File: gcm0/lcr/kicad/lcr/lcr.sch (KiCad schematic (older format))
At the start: 82 parts, among them Q1 BC547, Q2 BC547, Q3 BC547, Q4 BC547, Q5 BC547, SW1 SW_Push, SW2 SW_Push, U1 L7805, U10 NE5532, U10 TL084, U11 CD4053B, U2 L7905, U3 LM1117-3.3, U4 74HC595, U5 STM32F030F4P6, U7 CD4052B, U8 NE5532, U9 NE5532, Y1 8M

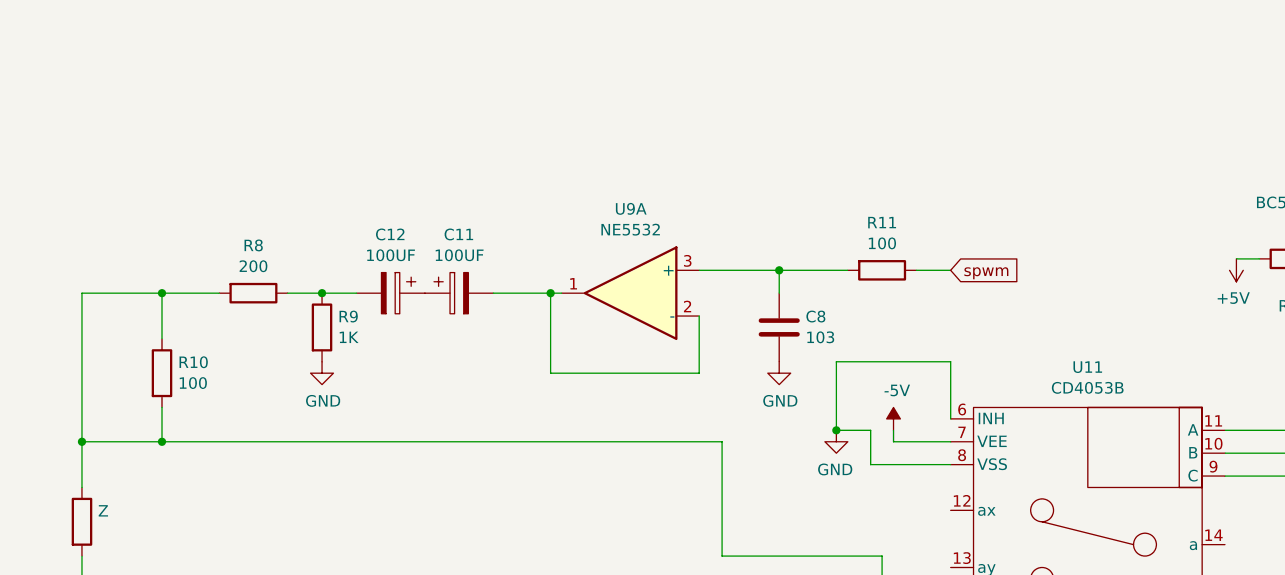
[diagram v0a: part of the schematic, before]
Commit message: 修改阻抗计算函数
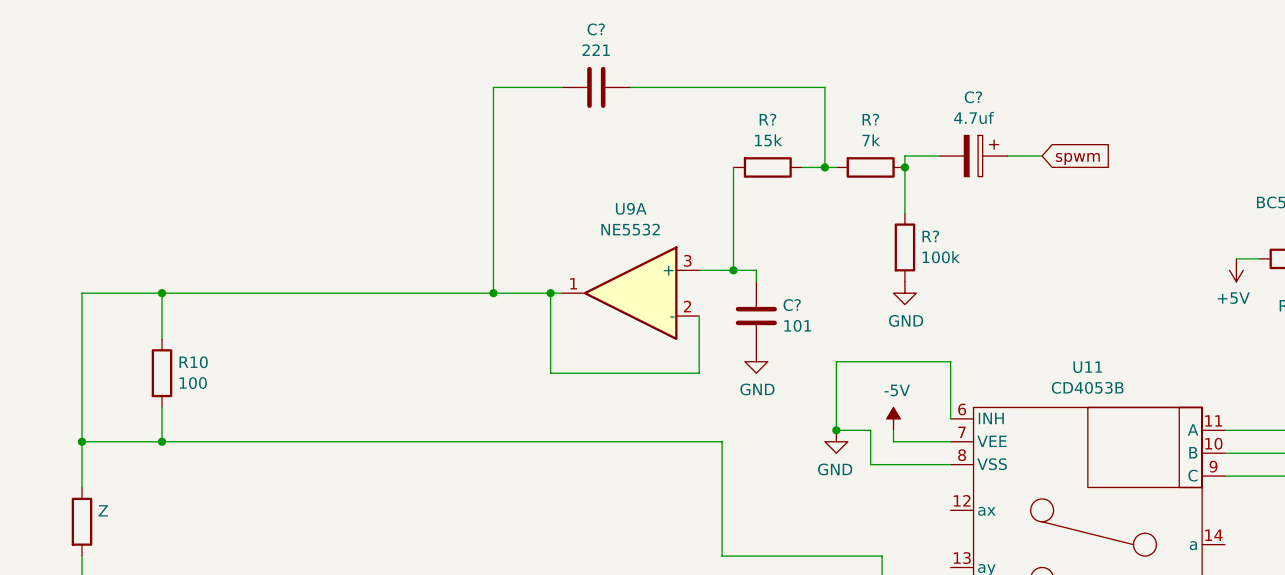
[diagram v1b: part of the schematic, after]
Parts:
- removed C11, C12: 100UF, symbol Device:CP
- removed C8: 103, symbol Device:C
- removed R11: 100, symbol Device:R
- removed R8: 200, symbol Device:R
- removed R9: 1K, symbol Device:R
- added C?: 101, symbol Device:C
- added C?: 221, symbol Device:C
- added C?: 4.7uf, symbol Device:CP
- added R?: 15k, symbol Device:R
- added R?: 7k, symbol Device:R
- added R?: 100k, symbol Device:R
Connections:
- net GND: now also C?.2, R?.2
- net spwm: now also C?.1
- net at R10.1, R10.2, U11.2 (bx)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: now also U9.1, U9.2 (-), C?.2
- net at U9.3 (+): now also C?.1, R?.2
- new net: C?.1, R?.1, R?.2
- new net: C?.2, R?.1, R?.1
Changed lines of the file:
@@
 	1250 2300 1250 2450
 Connection ~ 2050 3150
-$Comp
-L Device:CP C11
-U 1 1 5DB73CA6
-P 2550 1800
-F 0 "C11" V 2295 1800 50  0000 C CNN
-F 1 "100UF" V 2386 1800 50  0000 C CNN
-F 2 "" H 2588 1650 50  0001 C CNN
-F 3 "~" H 2550 1800 50  0001 C CNN
-	1    2550 1800
-	0    -1   1    0
-$EndComp
-$Comp
-L Device:CP C12
-U 1 1 5DB75C4D
-P 2250 1800
-F 0 "C12" V 1995 1800 50  0000 C CNN
-F 1 "100UF" V 2086 1800 50  0000 C CNN
-F 2 "" H 2288 1650 50  0001 C CNN
-F 3 "~" H 2250 1800 50  0001 C CNN
-	1    2250 1800
-	0    1    1    0
-$EndComp
 Wire Wire Line
 	3000 1800 2950 1800
-$Comp
-L Device:R R9
-U 1 1 5DBA1D7C
-P 1950 1950
-F 0 "R9" H 2020 1996 50  0000 L CNN
-F 1 "1K" H 2020 1905 50  0000 L CNN
-F 2 "" V 1880 1950 50  0001 C CNN
-F 3 "~" H 1950 1950 50  0001 C CNN
-	1    1950 1950
-	1    0    0    -1
-$EndComp
-$Comp
-L Device:R R8
-U 1 1 5DBA3300
-P 1650 1800
-F 0 "R8" V 1443 1800 50  0000 C CNN
-F 1 "200" V 1534 1800 50  0000 C CNN
-F 2 "" V 1580 1800 50  0001 C CNN
-F 3 "~" H 1650 1800 50  0001 C CNN
-	1    1650 1800
-	0    1    1    0
-$EndComp
-Wire Wire Line
-	2100 1800 1950 1800
-Wire Wire Line
-	1950 1800 1800 1800
-Connection ~ 1950 1800
 Wire Wire Line
 	3600 1900 3600 2150
@@
 $Comp
 L power:GND #PWR?
-U 1 1 5DBEFC51
-P 1950 2100
-F 0 "#PWR?" H 1950 1850 50  0001 C CNN
-F 1 "GND" H 1955 1927 50  0000 C CNN
-F 2 "" H 1950 2100 50  0001 C CNN
-F 3 "" H 1950 2100 50  0001 C CNN
-	1    1950 2100
-	1    0    0    -1
-$EndComp
-$Comp
-L power:GND #PWR?
 U 1 1 5DBF1737
-P 3950 2100
-F 0 "#PWR?" H 3950 1850 50  0001 C CNN
-F 1 "GND" H 3955 1927 50  0000 C CNN
-F 2 "" H 3950 2100 50  0001 C CNN
-F 3 "" H 3950 2100 50  0001 C CNN
-	1    3950 2100
-	1    0    0    -1
-$EndComp
-$Comp
-L Device:C C8
-U 1 1 5DBF3A78
-P 3950 1950
-F 0 "C8" H 4065 1996 50  0000 L CNN
-F 1 "103" H 4065 1905 50  0000 L CNN
-F 2 "" H 3988 1800 50  0001 C CNN
-F 3 "~" H 3950 1950 50  0001 C CNN
-	1    3950 1950
-	1    0    0    -1
-$EndComp
-Wire Wire Line
-	3600 1700 3950 1700
-Wire Wire Line
-	3950 1700 3950 1800
-$Comp
-L Device:R R11
-U 1 1 5DC0413C
-P 4400 1700
-F 0 "R11" V 4193 1700 50  0000 C CNN
-F 1 "100" V 4284 1700 50  0000 C CNN
-F 2 "" V 4330 1700 50  0001 C CNN
-F 3 "~" H 4400 1700 50  0001 C CNN
-	1    4400 1700
-	0    1    1    0
-$EndComp
-Wire Wire Line
-	4250 1700 3950 1700
-Connection ~ 3950 1700
-Wire Wire Line
-	1500 1800 1250 1800
+P 3850 2050
+F 0 "#PWR?" H 3850 1800 50  0001 C CNN
+F 1 "GND" H 3855 1877 50  0000 C CNN
+F 2 "" H 3850 2050 50  0001 C CNN
+F 3 "" H 3850 2050 50  0001 C CNN
+	1    3850 2050
+	1    0    0    -1
+$EndComp
 Wire Wire Line
 	1250 1800 1250 2000
-Text GLabel 4700 1700 2    50   Input ~ 0
+Text GLabel 5100 1200 2    50   Input ~ 0
 spwm
 Wire Wire Line
-	4700 1700 4550 1700
+	5100 1200 4950 1200
 Text GLabel 14700 8100 2    50   Input ~ 0
 ADC1
@@
 Wire Wire Line
 	900  1800 900  2450
-Connection ~ 1250 1800
 Wire Wire Line
 	1250 2450 900  2450
@@
 	12550 4000 12550 4250
 Connection ~ 12550 4250
+$Comp
+L Device:R R?
+U 1 1 5D991ACB
+P 3900 1250
+F 0 "R?" V 3693 1250 50  0000 C CNN
+F 1 "15k" V 3784 1250 50  0000 C CNN
+F 2 "" V 3830 1250 50  0001 C CNN
+F 3 "~" H 3900 1250 50  0001 C CNN
+	1    3900 1250
+	0    1    1    0
+$EndComp
+$Comp
+L Device:R R?
+U 1 1 5D993C65
+P 4350 1250
+F 0 "R?" V 4143 1250 50  0000 C CNN
+F 1 "7k" V 4234 1250 50  0000 C CNN
+F 2 "" V 4280 1250 50  0001 C CNN
+F 3 "~" H 4350 1250 50  0001 C CNN
+	1    4350 1250
+	0    1    1    0
+$EndComp
+$Comp
+L Device:R R?
+U 1 1 5D9B1D5F
+P 4500 1600
+F 0 "R?" H 4570 1646 50  0000 L CNN
+F 1 "100k" H 4570 1555 50  0000 L CNN
+F 2 "" V 4430 1600 50  0001 C CNN
+F 3 "~" H 4500 1600 50  0001 C CNN
+	1    4500 1600
+	1    0    0    -1
+$EndComp
+$Comp
+L Device:C C?
+U 1 1 5D9E9F87
+P 3850 1900
+F 0 "C?" H 3965 1946 50  0000 L CNN
+F 1 "101" H 3965 1855 50  0000 L CNN
+F 2 "" H 3888 1750 50  0001 C CNN
+F 3 "~" H 3850 1900 50  0001 C CNN
+	1    3850 1900
+	1    0    0    -1
+$EndComp
+Wire Wire Line
+	3850 1700 3850 1750
+Wire Wire Line
+	3750 1250 3750 1700
+Wire Wire Line
+	3600 1700 3750 1700
+Connection ~ 3750 1700
+Wire Wire Line
+	3750 1700 3850 1700
+Wire Wire Line
+	4050 1250 4150 1250
+Wire Wire Line
+	4500 1250 4500 1450
+$Comp
+L Device:C C?
+U 1 1 5DA7AEC8
+P 3150 900
+F 0 "C?" V 2898 900 50  0000 C CNN
+F 1 "221" V 2989 900 50  0000 C CNN
+F 2 "" H 3188 750 50  0001 C CNN
+F 3 "~" H 3150 900 50  0001 C CNN
+	1    3150 900
+	0    1    1    0
+$EndComp
+Wire Wire Line
+	3300 900  4150 900
+Wire Wire Line
+	4150 900  4150 1250
+Connection ~ 4150 1250
+Wire Wire Line
+	4150 1250 4200 1250
+Wire Wire Line
+	3000 900  2700 900
+Wire Wire Line
+	2700 900  2700 1800
+Wire Wire Line
+	1250 1800 2700 1800
+Connection ~ 1250 1800
+Connection ~ 2700 1800
+$Comp
+L Device:CP C?
+U 1 1 5DAF3F4F
+P 4800 1200
+F 0 "C?" V 4545 1200 50  0000 C CNN
+F 1 "4.7uf" V 4636 1200 50  0000 C CNN
+F 2 "" H 4838 1050 50  0001 C CNN
+F 3 "~" H 4800 1200 50  0001 C CNN
+	1    4800 1200
+	0    1    1    0
+$EndComp
+Wire Wire Line
+	4650 1200 4500 1200
+Wire Wire Line
+	4500 1200 4500 1250
+Connection ~ 4500 1250
+$Comp
+L power:GND #PWR?
+U 1 1 5DB3405A
+P 4500 1750
+F 0 "#PWR?" H 4500 1500 50  0001 C CNN
+F 1 "GND" H 4505 1577 50  0000 C CNN
+F 2 "" H 4500 1750 50  0001 C CNN
+F 3 "" H 4500 1750 50  0001 C CNN
+	1    4500 1750
+	1    0    0    -1
+$EndComp
 $EndSCHEMATC

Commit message: 试验设置几个量程
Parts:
- added R8: 390, symbol Device:R
- R17: value 1k -> 390
- gave numbers to parts that had none: 6
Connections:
- net at R10.1, R10.2, U11.2 (bx)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: now also R8.2; no longer C12.2, U9.1, U9.2 (-)
- new net: C12.2, R8.1, U9.1, U9.2 (-)
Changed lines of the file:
@@
 P 2300 4600
 F 0 "R17" V 2507 4600 50  0000 C CNN
-F 1 "1k" V 2416 4600 50  0000 C CNN
+F 1 "390" V 2416 4600 50  0000 C CNN
 F 2 "" V 2230 4600 50  0001 C CNN
 F 3 "~" H 2300 4600 50  0001 C CNN
@@
 Connection ~ 1250 3150
 Wire Wire Line
-	900  1800 1250 1800
-Wire Wire Line
 	900  1800 900  2450
 Wire Wire Line
@@
 Connection ~ 12550 4250
 $Comp
-L Device:R R?
+L Device:R R36
 U 1 1 5D991ACB
 P 3900 1250
-F 0 "R?" V 3693 1250 50  0000 C CNN
+F 0 "R36" V 3693 1250 50  0000 C CNN
 F 1 "15k" V 3784 1250 50  0000 C CNN
 F 2 "" V 3830 1250 50  0001 C CNN
@@
 $EndComp
 $Comp
-L Device:R R?
+L Device:R R11
 U 1 1 5D993C65
 P 4350 1250
-F 0 "R?" V 4143 1250 50  0000 C CNN
+F 0 "R11" V 4143 1250 50  0000 C CNN
 F 1 "7k" V 4234 1250 50  0000 C CNN
 F 2 "" V 4280 1250 50  0001 C CNN
@@
 $EndComp
 $Comp
-L Device:R R?
+L Device:R R37
 U 1 1 5D9B1D5F
 P 4500 1600
-F 0 "R?" H 4570 1646 50  0000 L CNN
+F 0 "R37" H 4570 1646 50  0000 L CNN
 F 1 "100k" H 4570 1555 50  0000 L CNN
 F 2 "" V 4430 1600 50  0001 C CNN
@@
 $EndComp
 $Comp
-L Device:C C?
+L Device:C C8
 U 1 1 5D9E9F87
 P 3850 1900
-F 0 "C?" H 3965 1946 50  0000 L CNN
+F 0 "C8" H 3965 1946 50  0000 L CNN
 F 1 "101" H 3965 1855 50  0000 L CNN
 F 2 "" H 3888 1750 50  0001 C CNN
@@
 	4500 1250 4500 1450
 $Comp
-L Device:C C?
+L Device:C C12
 U 1 1 5DA7AEC8
 P 3150 900
-F 0 "C?" V 2898 900 50  0000 C CNN
+F 0 "C12" V 2898 900 50  0000 C CNN
 F 1 "221" V 2989 900 50  0000 C CNN
 F 2 "" H 3188 750 50  0001 C CNN
@@
 Wire Wire Line
 	2700 900  2700 1800
-Wire Wire Line
-	1250 1800 2700 1800
-Connection ~ 1250 1800
-Connection ~ 2700 1800
-$Comp
-L Device:CP C?
+$Comp
+L Device:CP C11
 U 1 1 5DAF3F4F
 P 4800 1200
-F 0 "C?" V 4545 1200 50  0000 C CNN
+F 0 "C11" V 4545 1200 50  0000 C CNN
 F 1 "4.7uf" V 4636 1200 50  0000 C CNN
 F 2 "" H 4838 1050 50  0001 C CNN
@@
 	1    0    0    -1
 $EndComp
+$Comp
+L Device:R R8
+U 1 1 5D8F52C3
+P 2000 1800
+F 0 "R8" V 1793 1800 50  0000 C CNN
+F 1 "390" V 1884 1800 50  0000 C CNN
+F 2 "" V 1930 1800 50  0001 C CNN
+F 3 "~" H 2000 1800 50  0001 C CNN
+	1    2000 1800
+	0    1    1    0
+$EndComp
+Wire Wire Line
+	2150 1800 2700 1800
+Connection ~ 2700 1800
+Wire Wire Line
+	900  1800 1250 1800
+Connection ~ 1250 1800
+Wire Wire Line
+	1250 1800 1850 1800
 $EndSCHEMATC
